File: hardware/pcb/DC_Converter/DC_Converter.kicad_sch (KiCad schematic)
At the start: 8 parts

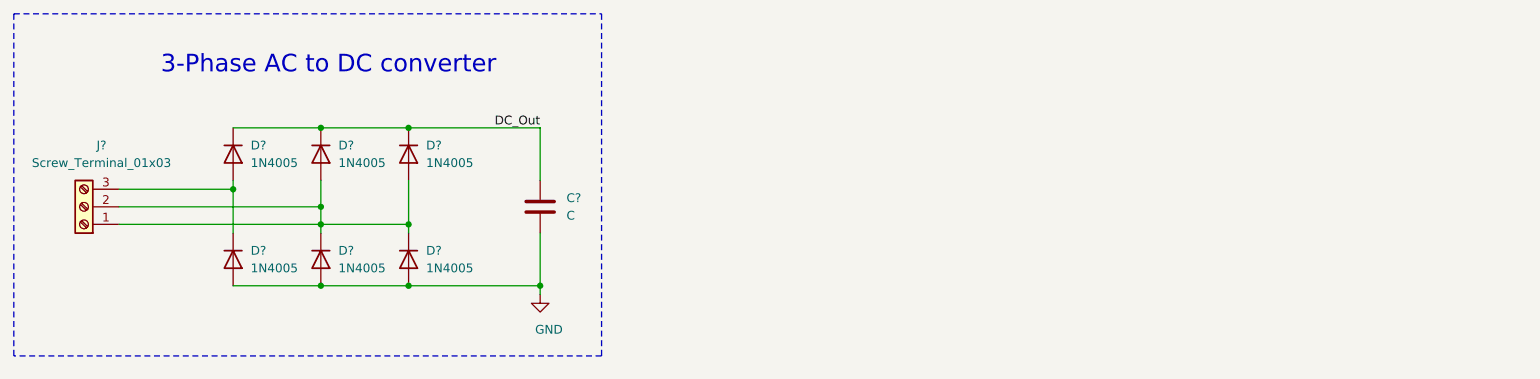
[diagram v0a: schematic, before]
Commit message: added voltage and current sensing to schematic
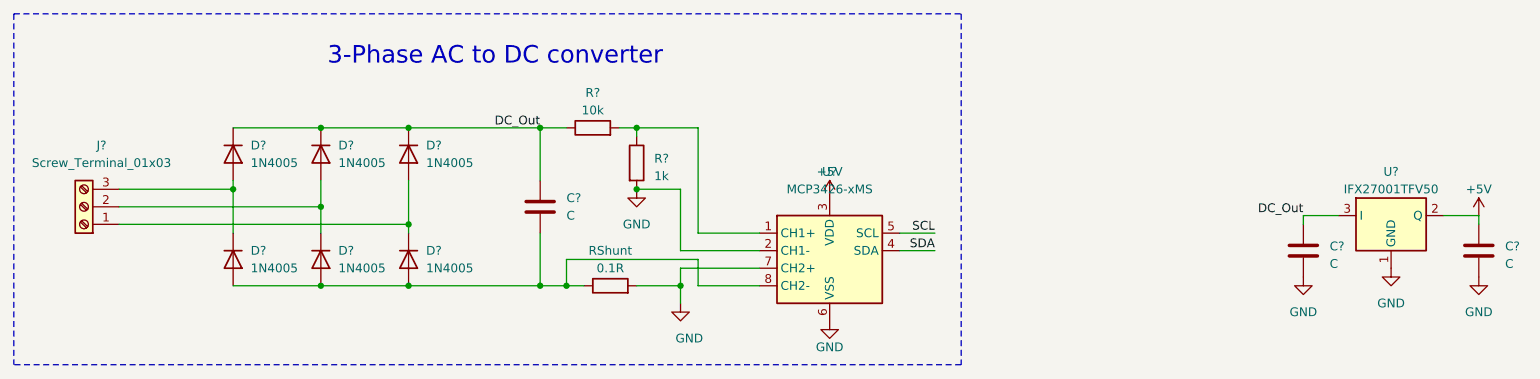
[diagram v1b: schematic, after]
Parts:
- added C? (x2): C, symbol Device:C
- added R?: 1k, symbol Device:R
- added R?: 10k, symbol Device:R
- added RShunt: 0.1R, symbol Device:R
- added U?: MCP3426-xMS, symbol Analog_ADC:MCP3426-xMS
- added U?: IFX27001TFV50, Package_TO_SOT_SMD:TO-252-3_TabPin2, symbol Regulator_Linear:IFX27001TFV50
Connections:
- net DC_Out: now also C?.1, R?.1, U?.3 (I)
- net GND: now also C?.2, C?.2, R?.2, RShunt.2, U?.1 (GND), U?.2 (CH1-), U?.6 (VSS), U?.7 (CH2+); no longer C?.2, D?.2 (A), D?.2 (A), D?.2 (A)
- net at D?.1 (K), D?.2 (A), J?.1 (Pin_1): no longer D?.1 (K), D?.2 (A), J?.2 (Pin_2)
- new net: R?.1, R?.2, U?.1 (CH1+)
- new net: C?.2, D?.2 (A), D?.2 (A), D?.2 (A), RShunt.1, U?.8 (CH2-)
- new net: D?.1 (K), D?.2 (A), J?.2 (Pin_2)
- new net +5V: C?.1, U?.2 (Q), U?.3 (VDD)
- new net SCL: U?.5 (SCL)
- new net SDA: U?.4 (SDA)
